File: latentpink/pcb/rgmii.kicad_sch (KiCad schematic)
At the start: 1 part, among them U2 XC7K160T-2FBG484C

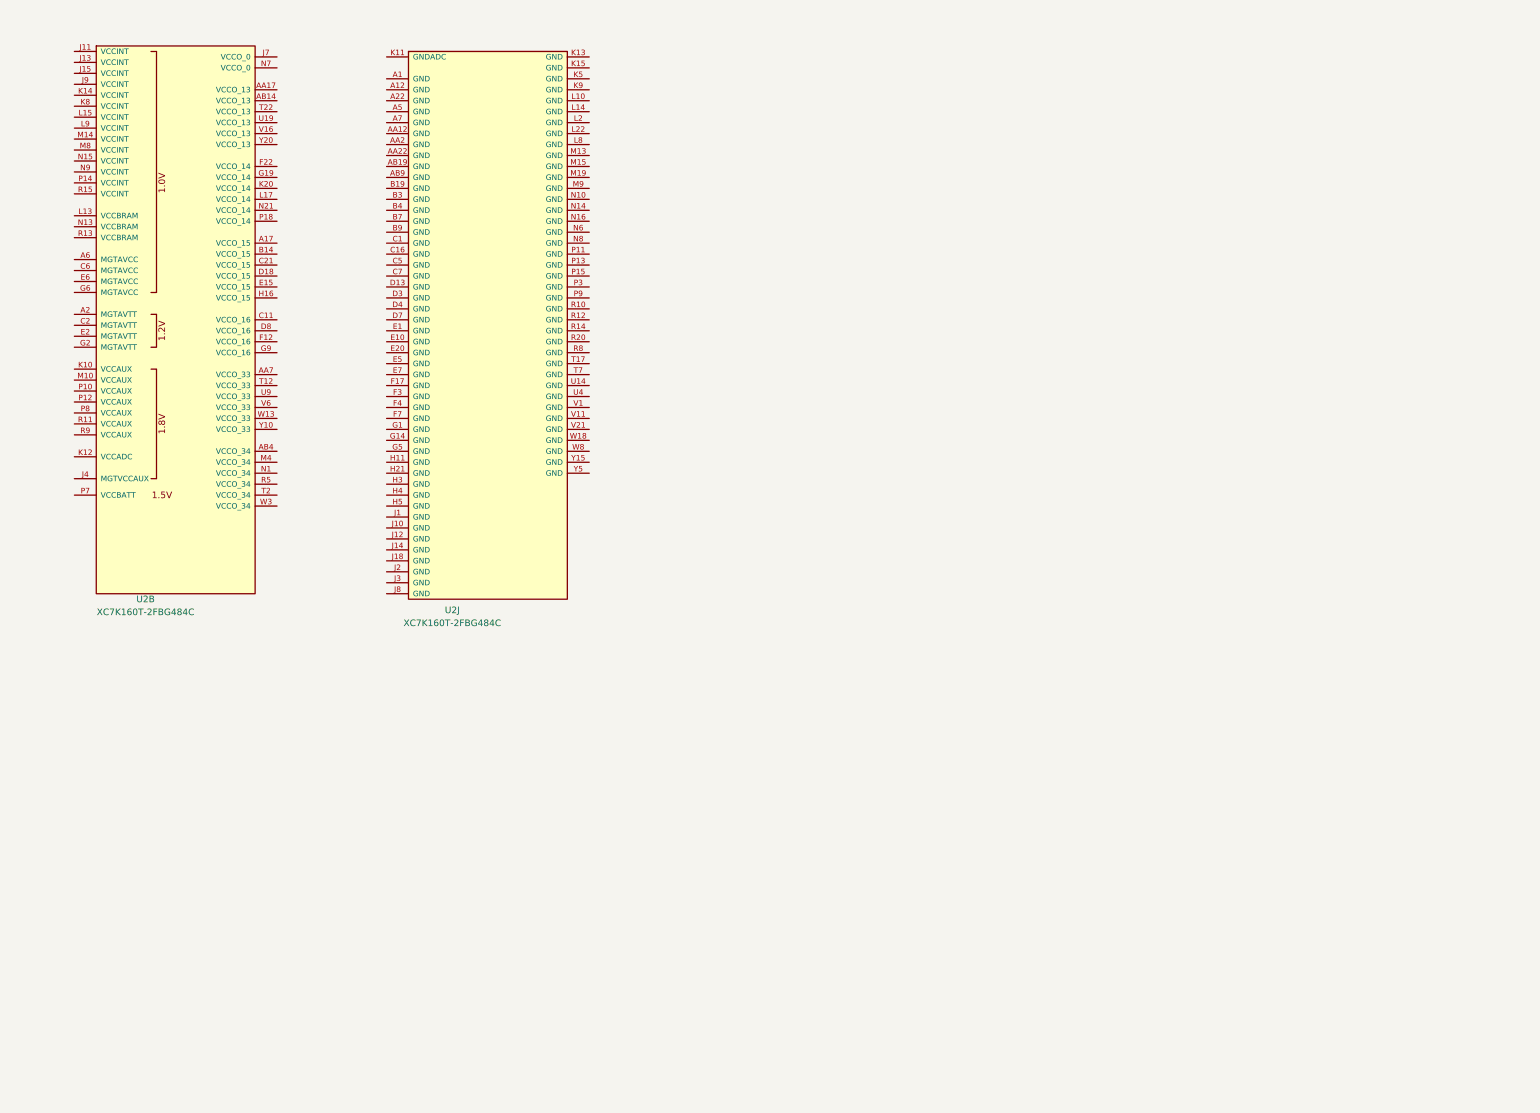
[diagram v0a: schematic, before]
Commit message: Continued initial schematic capture
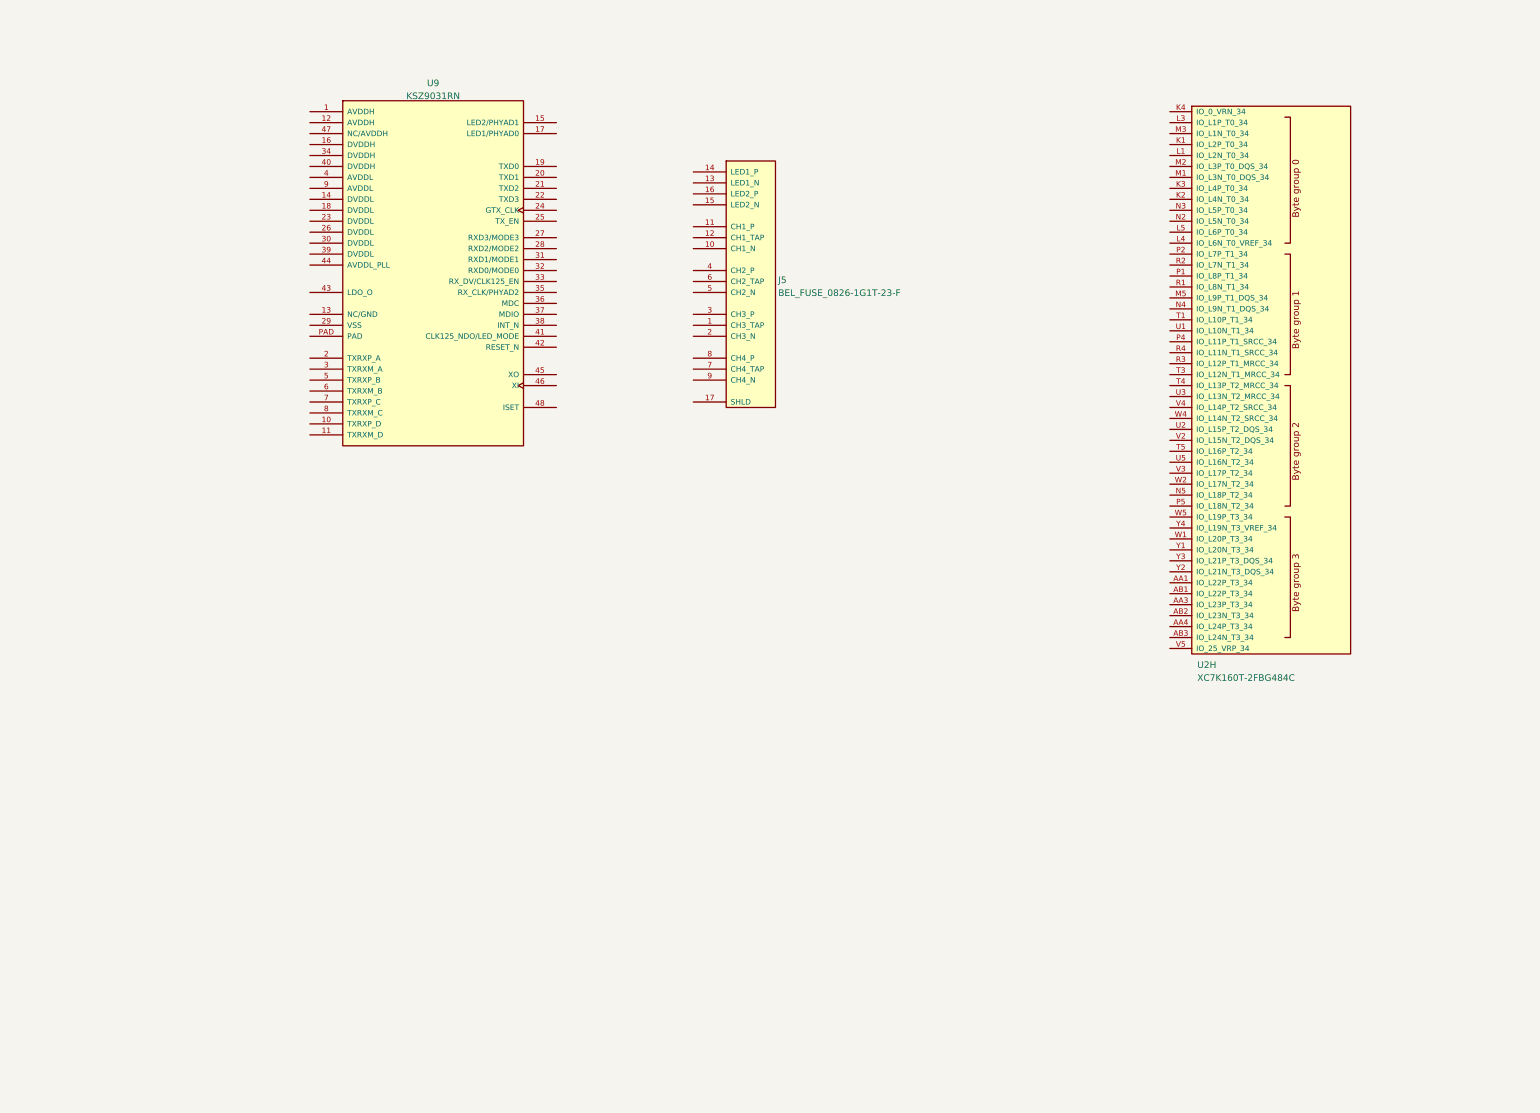
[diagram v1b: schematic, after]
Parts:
- removed U2: XC7K160T-2FBG484C, azonenberg_pcb:BGA_484_22x22_FULLARRAY_1MM, symbol xilinx-azonenberg:XC7KxT-FBG484
- added J5: BEL_FUSE_0826-1G1T-23-F, azonenberg_pcb:CONN_BELFUSE_0826_1G1T_23_F, symbol special-azonenberg:BEL_FUSE_0826-1G1T-23-F
- added U2: XC7K160T-2FBG484C, azonenberg_pcb:BGA_484_22x22_FULLARRAY_1MM, symbol xilinx-azonenberg:XC7KxT-FBG484
- added U9: KSZ9031RN, azonenberg_pcb:QFN_48_0.5MM_7x7MM, symbol special-azonenberg:KSZ9031RN
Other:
- company: Antikernel Labs -> (none)

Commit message: Initial version of RGMII PHY schematic
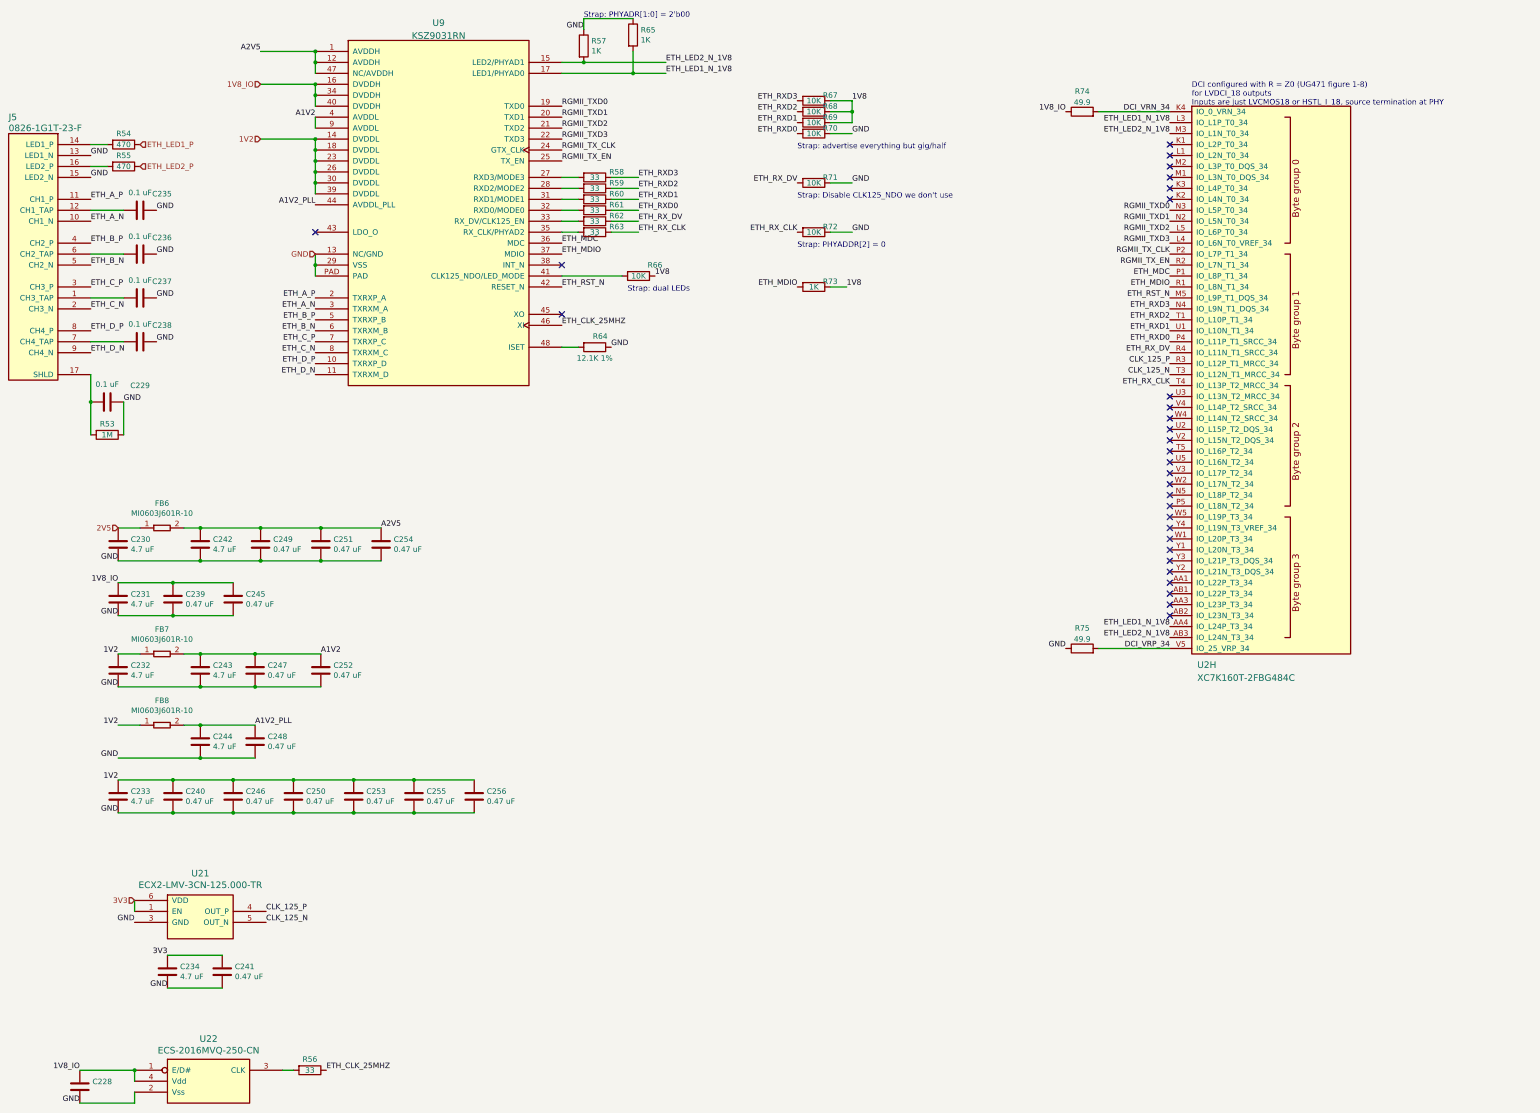
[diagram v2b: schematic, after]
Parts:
- added C228: ~, symbol device:C
- added C229, C235, C236, C237, C238: 0.1 uF, azonenberg_pcb:EIA_0402_CAP_NOSILK, symbol device:C
- added C230, C231, C232, C233, C242, C243, C244: 4.7 uF, azonenberg_pcb:EIA_0603_CAP_NOSILK, symbol device:C
- added C234: 4.7 uF, symbol device:C
- added C239, C240, C245, C246, C247, C248, C249, C250, C251, C252, C253, C254, C255, C256: 0.47 uF, azonenberg_pcb:EIA_0402_CAP_NOSILK, symbol device:C
- added C241: 0.47 uF, symbol device:C
- added FB6, FB7, FB8: MI0603J601R-10, azonenberg_pcb:EIA_0603_INDUCTOR_NOSILK, symbol passive-azonenberg:FERRITE_SMALL2
- added R53: 1M, azonenberg_pcb:EIA_0402_RES_NOSILK, symbol device:R
- added R54, R55: 470, azonenberg_pcb:EIA_0402_RES_NOSILK, symbol device:R
- added R56, R58, R59, R60, R61, R62, R63: 33, azonenberg_pcb:EIA_0402_RES_NOSILK, symbol device:R
- added R57, R65, R73: 1K, azonenberg_pcb:EIA_0402_RES_NOSILK, symbol device:R
- added R64: 12.1K 1%, azonenberg_pcb:EIA_0402_RES_NOSILK, symbol device:R
- added R66, R67, R68, R69, R70, R71, R72: 10K, azonenberg_pcb:EIA_0402_RES_NOSILK, symbol device:R
- added R74, R75: 49.9, symbol device:R
- added U21: ECX2-LMV-3CN-125.000-TR, symbol osc-azonenberg:OSC_LVDS_NOPAD
- added U22: ECS-2016MVQ-250-CN, azonenberg_pcb:OSCILLATOR_2.0x1.6, symbol osc-azonenberg:OSC
- J5: value BEL_FUSE_0826-1G1T-23-F -> 0826-1G1T-23-F
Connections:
- net at J5.1 (CH3_TAP): now also C237.2
- net ETH_A_N: now reaches J5.10 (CH1_N)
- net ETH_A_N: now also U9.3 (TXRXM_A)
- net ETH_A_P: now reaches J5.11 (CH1_P)
- net ETH_A_P: now also U9.2 (TXRXP_A)
- net at J5.12 (CH1_TAP): now also C235.2
- net GND: now reaches J5.13 (LED1_N)
- net GND: now also J5.15 (LED2_N), U9.13 (NC/GND), U9.29 (VSS), U9.PAD, C228.2, C229.1, C230.2, C231.2, C232.2, C233.2, C234.2, C235.1, C236.1, C237.1, C238.1, C239.2, C240.2, C241.2, C242.2, C243.2, C244.2, C245.2, C246.2, C247.2, C248.2, C249.2, C250.2, C251.2, C252.2, C253.2, C254.2, C255.2, C256.2, R53.1, R57.1, R64.1, R65.1, R70.1, R71.1, R72.1, R75.1, U21.3 (GND), U22.2 (Vss)
- net at J5.14 (LED1_P): now also R54.2
- net at J5.16 (LED2_P): now also R55.2
- net at J5.17 (SHLD): now also C229.2, R53.2
- net ETH_C_N: now reaches J5.2 (CH3_N)
- net ETH_C_N: now also U9.8 (TXRXM_C)
- net ETH_C_P: now reaches J5.3 (CH3_P)
- net ETH_C_P: now also U9.7 (TXRXP_C)
- net ETH_B_P: now reaches J5.4 (CH2_P)
- net ETH_B_P: now also U9.5 (TXRXP_B)
- net ETH_B_N: now reaches J5.5 (CH2_N)
- net ETH_B_N: now also U9.6 (TXRXM_B)
- net at J5.6 (CH2_TAP): now also C236.2
- net at J5.7 (CH4_TAP): now also C238.2
- net ETH_D_P: now reaches J5.8 (CH4_P)
- net ETH_D_P: now also U9.10 (TXRXP_D)
- net ETH_D_N: now reaches J5.9 (CH4_N)
- net ETH_D_N: now also U9.11 (TXRXM_D)
- net ETH_LED1_N_1V8: now reaches U2.AA4 (IO_L24P_T3_34)
- net ETH_LED1_N_1V8: now also U2.L3 (IO_L1P_T0_34), U9.17 (LED1/PHYAD0), R65.2
- net ETH_LED2_N_1V8: now reaches U2.AB3 (IO_L24N_T3_34)
- net ETH_LED2_N_1V8: now also U2.M3 (IO_L1N_T0_34), U9.15 (LED2/PHYAD1), R57.2
- net DCI_VRN_34: now reaches U2.K4 (IO_0_VRN_34)
- net DCI_VRN_34: now also R74.2
- net RGMII_TXD3: now reaches U2.L4 (IO_L6N_T0_VREF_34)
- net RGMII_TXD3: now also U9.22 (TXD3)
- net RGMII_TXD2: now reaches U2.L5 (IO_L6P_T0_34)
- net RGMII_TXD2: now also U9.21 (TXD2)
- net ETH_RST_N: now reaches U2.M5 (IO_L9P_T1_DQS_34)
- net ETH_RST_N: now also U9.42 (RESET_N)
- net RGMII_TXD1: now reaches U2.N2 (IO_L5N_T0_34)
- net RGMII_TXD1: now also U9.20 (TXD1)
- net RGMII_TXD0: now reaches U2.N3 (IO_L5P_T0_34)
- net RGMII_TXD0: now also U9.19 (TXD0)
- net ETH_RXD3: now reaches U2.N4 (IO_L9N_T1_DQS_34)
- net ETH_RXD3: now also R58.1, R67.2
- net ETH_MDC: now reaches U2.P1 (IO_L8P_T1_34)
- net ETH_MDC: now also U9.36 (MDC)
- net RGMII_TX_CLK: now reaches U2.P2 (IO_L7P_T1_34)
- net RGMII_TX_CLK: now also U9.24 (GTX_CLK)
- net ETH_RXD0: now reaches U2.P4 (IO_L11P_T1_SRCC_34)
- net ETH_RXD0: now also R61.1, R70.2
- net ETH_MDIO: now reaches U2.R1 (IO_L8N_T1_34)
- net ETH_MDIO: now also U9.37 (MDIO), R73.2
- net RGMII_TX_EN: now reaches U2.R2 (IO_L7N_T1_34)
- net RGMII_TX_EN: now also U9.25 (TX_EN)
- net CLK_125_P: now reaches U2.R3 (IO_L12P_T1_MRCC_34)
- net CLK_125_P: now also U21.4 (OUT_P)
- net ETH_RX_DV: now reaches U2.R4 (IO_L11N_T1_SRCC_34)
- net ETH_RX_DV: now also R62.1, R71.2
- net ETH_RXD2: now reaches U2.T1 (IO_L10P_T1_34)
- net ETH_RXD2: now also R59.1, R68.2
- net CLK_125_N: now reaches U2.T3 (IO_L12N_T1_MRCC_34)
- net CLK_125_N: now also U21.5 (OUT_N)
- net ETH_RX_CLK: now reaches U2.T4 (IO_L13P_T2_MRCC_34)
- net ETH_RX_CLK: now also R63.1, R72.2
- net ETH_RXD1: now reaches U2.U1 (IO_L10N_T1_34)
- net ETH_RXD1: now also R60.1, R69.2
- net DCI_VRP_34: now reaches U2.V5 (IO_25_VRP_34)
- net DCI_VRP_34: now also R75.2
- net A2V5: now reaches U9.1 (AVDDH)
- net A2V5: now also U9.12 (AVDDH), U9.47 (NC/AVDDH), C242.1, C249.1, C251.1, C254.1, FB6.2
- net 1V2: now reaches U9.14 (DVDDL)
- net 1V2: now also U9.18 (DVDDL), U9.23 (DVDDL), U9.26 (DVDDL), U9.30 (DVDDL), U9.39 (DVDDL), C232.1, C233.1, C240.1, C246.1, C250.1, C253.1, C255.1, C256.1, FB7.1, FB8.1
- net 1V8_IO: now reaches U9.16 (DVDDH)
- net 1V8_IO: now also U9.34 (DVDDH), U9.40 (DVDDH), C228.1, C231.1, C239.1, C245.1, R74.1, U22.1 (E/D#), U22.4 (Vdd)
- net at U9.27 (RXD3/MODE3): now also R58.2
- net at U9.28 (RXD2/MODE2): now also R59.2
- net at U9.31 (RXD1/MODE1): now also R60.2
- net at U9.32 (RXD0/MODE0): now also R61.2
- net at U9.33 (RX_DV/CLK125_EN): now also R62.2
- net at U9.35 (RX_CLK/PHYAD2): now also R63.2
- net A1V2: now reaches U9.4 (AVDDL)
- net A1V2: now also U9.9 (AVDDL), C243.1, C247.1, C252.1, FB7.2
- net at U9.41 (CLK125_NDO/LED_MODE): now also R66.2
- net A1V2_PLL: now reaches U9.44 (AVDDL_PLL)
- net A1V2_PLL: now also C244.1, C248.1, FB8.2
- net ETH_CLK_25MHZ: now reaches U9.46 (XI)
- net ETH_CLK_25MHZ: now also R56.1
- net at U9.48 (ISET): now also R64.2
- new net: R56.2, U22.3 (CLK)
- new net 1V8: R66.1, R67.1, R68.1, R69.1, R73.1
- new net 2V5: C230.1, FB6.1
- new net 3V3: C234.1, C241.1, U21.1 (EN), U21.6 (VDD)
- new net ETH_LED1_P: R54.1
- new net ETH_LED2_P: R55.1
- no-connect marks 0 -> 30
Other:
- note added: "DCI configured with R = Z0 (UG471 figure 1-8) for LVDCI_18 outputs Inputs are just LVCMOS18 or HSTL_I_18, source termination at PHY"
- note added: "Strap: Disable CLK125_NDO we don't use"
- note added: "Strap: PHYADDR[2] = 0"
- note added: "Strap: PHYADR[1:0] = 2'b00"
- note added: "Strap: advertise everything but gig/half"
- note added: "Strap: dual LEDs"
- moved on the sheet: J5, U9

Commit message: Continued work on QSGMII subsystem
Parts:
- R74, R75: footprint (none) -> azonenberg_pcb:EIA_0402_RES_NOSILK
- U21: footprint (none) -> azonenberg_pcb:OSCILLATOR_LVDS_3.2x2.5
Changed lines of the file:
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@@
   (paper "A3")
   (title_block
-    (date "2023-05-10")
+    (date "2023-05-14")
   )
   (junction (at 95.25 53.34) (diameter 0) (color 0 0 0 0)
@@
     (property "Reference" "R74" (id 0) (at 273.05 34.6542 90))
     (property "Value" "49.9" (id 1) (at 273.05 37.1911 90))
-    (property "Footprint" "" (id 2) (at 273.05 41.148 90)
+    (property "Footprint" "azonenberg_pcb:EIA_0402_RES_NOSILK" (id 2) (at 273.05 41.148 90)
       (effects (font (size 1.27 1.27)) hide)
     )
@@
     (property "Reference" "R75" (id 0) (at 273.05 159.1142 90))
     (property "Value" "49.9" (id 1) (at 273.05 161.6511 90))
-    (property "Footprint" "" (id 2) (at 273.05 165.608 90)
+    (property "Footprint" "azonenberg_pcb:EIA_0402_RES_NOSILK" (id 2) (at 273.05 165.608 90)
       (effects (font (size 1.27 1.27)) hide)
     )
@@
       (effects (font (size 1.524 1.524)))
     )
-    (property "Footprint" "" (id 2) (at 60.96 231.14 0)
+    (property "Footprint" "azonenberg_pcb:OSCILLATOR_LVDS_3.2x2.5" (id 2) (at 60.96 231.14 0)
       (effects (font (size 1.524 1.524)) hide)
     )

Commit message: Continued initial component placement
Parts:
- removed C229: 0.1 uF, azonenberg_pcb:EIA_0402_CAP_NOSILK, symbol device:C
- removed R53: 1M, azonenberg_pcb:EIA_0402_RES_NOSILK, symbol device:R
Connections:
- net CHGND: now reaches J5.17 (SHLD)
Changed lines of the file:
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@@
   (junction (at 95.25 48.26) (diameter 0) (color 0 0 0 0)
-  )
-  (junction (at 43.18 106.68) (diameter 0) (color 0 0 0 0)
   )
   (junction (at 68.58 165.1) (diameter 0) (color 0 0 0 0)
@@
     (stroke (width 0) (type default) (color 0 0 0 0))
   )
-  (wire (pts (xy 43.18 106.68) (xy 43.18 114.3))
-    (stroke (width 0) (type default) (color 0 0 0 0))
-  )
   (wire (pts (xy 43.18 46.99) (xy 46.99 46.99))
     (stroke (width 0) (type default) (color 0 0 0 0))
@@
   )
   (wire (pts (xy 62.23 156.21) (xy 76.2 156.21))
-    (stroke (width 0) (type default) (color 0 0 0 0))
-  )
-  (wire (pts (xy 50.8 106.68) (xy 50.8 114.3))
-    (stroke (width 0) (type default) (color 0 0 0 0))
-  )
-  (wire (pts (xy 43.18 100.33) (xy 43.18 106.68))
     (stroke (width 0) (type default) (color 0 0 0 0))
   )
@@
     (effects (font (size 1.27 1.27)) (justify left bottom))
   )
-  (label "GND" (at 50.8 106.68 0)
-    (effects (font (size 1.27 1.27)) (justify left bottom))
-  )
   (label "ETH_LED2_N_1V8" (at 293.37 44.45 180)
     (effects (font (size 1.27 1.27)) (justify right bottom))
@@
   (hierarchical_label "1V2" (shape input) (at 82.55 45.72 180)
     (effects (font (size 1.27 1.27)) (justify right))
+  )
+  (hierarchical_label "CHGND" (shape input) (at 43.18 100.33 0)
+    (effects (font (size 1.27 1.27)) (justify left))
   )
   (hierarchical_label "ETH_LED2_P" (shape input) (at 54.61 52.07 0)
@@
     )
     (property "Datasheet" "" (id 3) (at 73.66 238.76 0)
-      (effects (font (size 1.27 1.27)) hide)
-    )
-    (pin "1")
-    (pin "2")
-  )
-  (symbol (lib_id "device:C") (at 46.99 106.68 270) (unit 1)
-    (in_bom yes) (on_board yes)
-    (property "Reference" "C229" (id 0) (at 54.61 102.87 90))
-    (property "Value" "0.1 uF" (id 1) (at 46.99 102.5906 90))
-    (property "Footprint" "azonenberg_pcb:EIA_0402_CAP_NOSILK" (id 2) (at 43.18 107.6452 0)
-      (effects (font (size 1.27 1.27)) hide)
-    )
-    (property "Datasheet" "" (id 3) (at 46.99 106.68 0)
       (effects (font (size 1.27 1.27)) hide)
     )
@@
       (effects (font (size 1.27 1.27)) hide)
     )
-    (pin "1")
-    (pin "2")
-  )
-  (symbol (lib_id "device:R") (at 46.99 114.3 270) (unit 1)
-    (in_bom yes) (on_board yes)
-    (property "Reference" "R53" (id 0) (at 46.99 111.76 90))
-    (property "Value" "1M" (id 1) (at 46.99 114.3 90))
-    (property "Footprint" "azonenberg_pcb:EIA_0402_RES_NOSILK" (id 2) (at 46.99 112.522 90)
-      (effects (font (size 1.27 1.27)) hide)
-    )
-    (property "Datasheet" "" (id 3) (at 46.99 114.3 0)
-      (effects (font (size 1.27 1.27)) hide)
-    )

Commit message: Continued footprint assignment and miscellaneous missing tidbits of schematic
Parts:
- C228: value ~ -> 0.47 uF; footprint (none) -> azonenberg_pcb:EIA_0402_CAP_NOSILK
- C234: footprint (none) -> azonenberg_pcb:EIA_0603_CAP_NOSILK
- C241: footprint (none) -> azonenberg_pcb:EIA_0402_CAP_NOSILK
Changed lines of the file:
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@@
   (paper "A3")
   (title_block
-    (date "2023-05-16")
+    (date "2023-05-20")
   )
   (junction (at 95.25 53.34) (diameter 0) (color 0 0 0 0)
@@
       (effects (font (size 1.27 1.27)) (justify left))
     )
-    (property "Footprint" "" (id 2) (at 74.6252 242.57 0)
+    (property "Footprint" "azonenberg_pcb:EIA_0402_CAP_NOSILK" (id 2) (at 74.6252 242.57 0)
       (effects (font (size 1.27 1.27)) hide)
     )
@@
       (effects (font (size 1.27 1.27)) (justify left))
     )
-    (property "Value" "~" (id 1) (at 43.561 266.573 0)
-      (effects (font (size 1.27 1.27)) (justify left))
-    )
-    (property "Footprint" "" (id 2) (at 41.6052 269.24 0)
+    (property "Value" "0.47 uF" (id 1) (at 43.561 266.573 0)
+      (effects (font (size 1.27 1.27)) (justify left))
+    )
+    (property "Footprint" "azonenberg_pcb:EIA_0402_CAP_NOSILK" (id 2) (at 41.6052 269.24 0)
       (effects (font (size 1.27 1.27)) hide)
     )
@@
       (effects (font (size 1.27 1.27)) (justify left))
     )
-    (property "Footprint" "" (id 2) (at 61.9252 242.57 0)
-      (effects (font (size 1.27 1.27)) hide)
-    )
+    (property "Footprint" "azonenberg_pcb:EIA_0603_CAP_NOSILK" (id 2) (at 61.9252 242.57 0)
+      (effects (font (size 1.27 1.27)) hide)
+    )
